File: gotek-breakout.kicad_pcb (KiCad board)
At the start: 2 copper layers, 90 x 20 mm, 4 parts, among them J1 FFC 10x1 0.5mm, J2 USB_A, J3 OLED, J4 Encoder

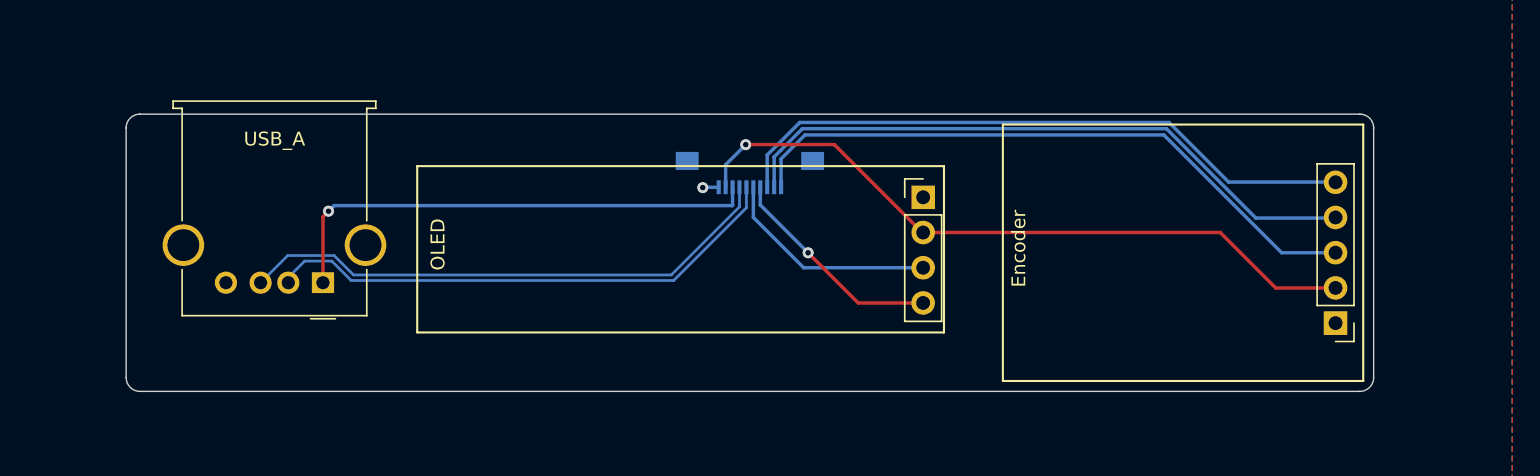
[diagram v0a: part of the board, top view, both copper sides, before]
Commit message: Make room for mounting
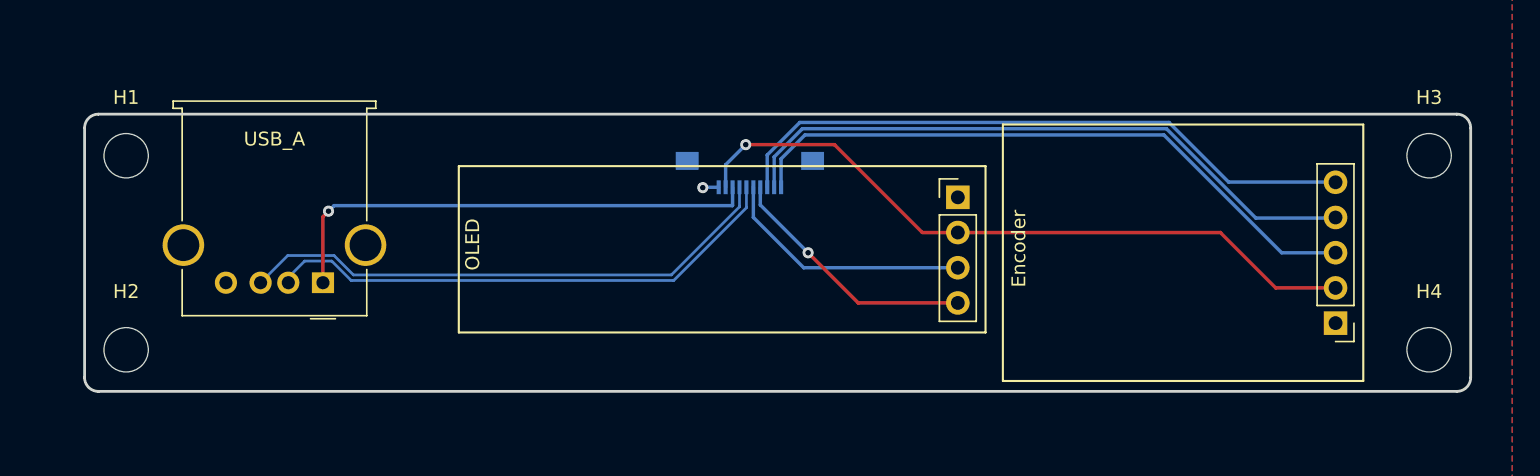
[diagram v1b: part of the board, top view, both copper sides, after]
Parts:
- added H1: MountingHole_3.2mm_M3, MountingHole:MountingHole_3.2mm_M3, F.Cu at (50.0, 43.0)
- added H2: MountingHole_3.2mm_M3, MountingHole:MountingHole_3.2mm_M3, F.Cu at (50.0, 57.0)
- added H3: MountingHole_3.2mm_M3, MountingHole:MountingHole_3.2mm_M3, F.Cu at (144.0, 43.0)
- added H4: MountingHole_3.2mm_M3, MountingHole:MountingHole_3.2mm_M3, F.Cu at (144.0, 57.0)
- moved J3 2.50 mm to (110.0, 46.0)
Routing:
- net /OLED_SCK: track 15.9 -> 18.4 mm
- net /OLED_SDA: track 16.0 -> 18.5 mm
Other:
- board size 90 x 20 mm -> 100 x 20 mm
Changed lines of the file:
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@@
     (pad "5" thru_hole circle (at 10.07 2.71 180) (size 3 3) (drill 2.3) (layers "*.Cu" "*.Mask")
       (net 1 "/GND") (pinfunction "Shield") (pintype "passive"))
-    (model "${KICAD6_3DMODEL_DIR}/Connector_USB.3dshapes/USB_A_Molex_67643_Horizontal.wrl"
-      (offset (xyz 0 0 0))
+    (model "${KICAD7_3DMODEL_DIR}/Connector_USB.3dshapes/USB_A_TE_292303-7_Horizontal.step"
+      (offset (xyz 3.5 -5.5 0))
       (scale (xyz 1 1 1))
       (rotate (xyz 0 0 0))
@@
     )
   )
+  (footprint "MountingHole:MountingHole_3.2mm_M3" (layer "F.Cu")
+    (at 50 43)
+    (descr "Mounting Hole 3.2mm, no annular, M3")
+    (tags "mounting hole 3.2mm no annular m3")
+    (clearance 1)
+    (attr board_only exclude_from_pos_files exclude_from_bom)
+    (fp_text reference "H1" (at 0 -4.2) (layer "F.SilkS")
+        (effects (font (size 1 1) (thickness 0.15)))
+    )
+    (fp_text value "MountingHole_3.2mm_M3" (at 0 4.2) (layer "F.Fab")
+        (effects (font (size 1 1) (thickness 0.15)))
+    )
+    (fp_text user "${REFERENCE}" (at 0 0) (layer "F.Fab")
+        (effects (font (size 1 1) (thickness 0.15)))
+    )
+    (fp_circle (center 0 0) (end 3.2 0)
+      (stroke (width 0.15) (type solid)) (fill none) (layer "Cmts.User"))
+    (fp_circle (center 0 0) (end 3.45 0)
+      (stroke (width 0.05) (type solid)) (fill none) (layer "F.CrtYd"))
+    (pad "" np_thru_hole circle (at 0 0) (size 3.2 3.2) (drill 3.2) (layers "*.Cu" "*.Mask"))
+  )
+  (footprint "MountingHole:MountingHole_3.2mm_M3" (layer "F.Cu")
+    (at 144 57)
+    (descr "Mounting Hole 3.2mm, no annular, M3")
+    (tags "mounting hole 3.2mm no annular m3")
+    (clearance 1)
+    (attr board_only exclude_from_pos_files exclude_from_bom)
+    (fp_text reference "H4" (at 0 -4.2) (layer "F.SilkS")
+        (effects (font (size 1 1) (thickness 0.15)))
+    )
+    (fp_text value "MountingHole_3.2mm_M3" (at 0 4.2) (layer "F.Fab")
+        (effects (font (size 1 1) (thickness 0.15)))
+    )
+    (fp_text user "${REFERENCE}" (at 0 0) (layer "F.Fab")
+        (effects (font (size 1 1) (thickness 0.15)))
+    )
+    (fp_circle (center 0 0) (end 3.2 0)
+      (stroke (width 0.15) (type solid)) (fill none) (layer "Cmts.User"))
+    (fp_circle (center 0 0) (end 3.45 0)
+      (stroke (width 0.05) (type solid)) (fill none) (layer "F.CrtYd"))
+    (pad "" np_thru_hole circle (at 0 0) (size 3.2 3.2) (drill 3.2) (layers "F&B.Cu" "*.Mask"))
+  )
   (footprint "Connector_PinHeader_2.54mm:PinHeader_1x04_P2.54mm_Vertical" (layer "F.Cu")
-    (at 107.5 46)
+    (at 110 46)
     (descr "Through hole straight pin header, 1x04, 2.54mm pitch, single row")
     (tags "Through hole pin header THT 1x04 2.54mm single row")
@@
       (rotate (xyz 0 0 0))
     )
+  )
+  (footprint "MountingHole:MountingHole_3.2mm_M3" (layer "F.Cu")
+    (at 144 43)
+    (descr "Mounting Hole 3.2mm, no annular, M3")
+    (tags "mounting hole 3.2mm no annular m3")
+    (clearance 1)
+    (attr board_only exclude_from_pos_files exclude_from_bom)
+    (fp_text reference "H3" (at 0 -4.2) (layer "F.SilkS")
+        (effects (font (size 1 1) (thickness 0.15)))
+    )
+    (fp_text value "MountingHole_3.2mm_M3" (at 0 4.2) (layer "F.Fab")
+        (effects (font (size 1 1) (thickness 0.15)))
+    )
+    (fp_text user "${REFERENCE}" (at 0 0) (layer "F.Fab")
+        (effects (font (size 1 1) (thickness 0.15)))
+    )
+    (fp_circle (center 0 0) (end 3.2 0)
+      (stroke (width 0.15) (type solid)) (fill none) (layer "Cmts.User"))
+    (fp_circle (center 0 0) (end 3.45 0)
+      (stroke (width 0.05) (type solid)) (fill none) (layer "F.CrtYd"))
+    (pad "" np_thru_hole circle (at 0 0) (size 3.2 3.2) (drill 3.2) (layers "*.Cu" "*.Mask"))
+  )
+  (footprint "MountingHole:MountingHole_3.2mm_M3" (layer "F.Cu")
+    (at 50 57)
+    (descr "Mounting Hole 3.2mm, no annular, M3")
+    (tags "mounting hole 3.2mm no annular m3")
+    (clearance 1)
+    (attr board_only exclude_from_pos_files exclude_from_bom)
+    (fp_text reference "H2" (at 0 -4.2) (layer "F.SilkS")
+        (effects (font (size 1 1) (thickness 0.15)))
+    )
+    (fp_text value "MountingHole_3.2mm_M3" (at 0 4.2) (layer "F.Fab")
+        (effects (font (size 1 1) (thickness 0.15)))
+    )
+    (fp_text user "${REFERENCE}" (at 0 0) (layer "F.Fab")
+        (effects (font (size 1 1) (thickness 0.15)))
+    )
+    (fp_circle (center 0 0) (end 3.2 0)
+      (stroke (width 0.15) (type solid)) (fill none) (layer "Cmts.User"))
+    (fp_circle (center 0 0) (end 3.45 0)
+      (stroke (width 0.05) (type solid)) (fill none) (layer "F.CrtYd"))
+    (pad "" np_thru_hole circle (at 0 0) (size 3.2 3.2) (drill 3.2) (layers "F&B.Cu" "*.Mask"))
   )
   (footprint "Connector_FFC-FPC:Molex_54548-1071_1x10-1MP_P0.5mm_Horizontal" (layer "B.Cu")
@@
     (pad "MP" smd rect (at -4.525 -0.875) (size 1.65 1.3) (layers "B.Cu" "B.Paste" "B.Mask"))
     (pad "MP" smd rect (at 4.525 -0.875) (size 1.65 1.3) (layers "B.Cu" "B.Paste" "B.Mask"))
-    (model "${KICAD6_3DMODEL_DIR}/Connector_FFC-FPC.3dshapes/Molex_54548-1071_1x10-1MP_P0.5mm_Horizontal.wrl"
-      (offset (xyz 0 0 0))
+    (model "${KICAD7_3DMODEL_DIR}/Connector_FFC-FPC.3dshapes/Hirose_FH12-10S-0.5SH_1x10-1MP_P0.50mm_Horizontal.step"
+      (offset (xyz 0 -0.5 0))
       (scale (xyz 1 1 1))
       (rotate (xyz 0 0 0))
     )
   )
-  (gr_rect (start 71 43.75) (end 109 55.75)
+  (gr_rect (start 74 43.75) (end 112 55.75)
     (stroke (width 0.15) (type default)) (fill none) (layer "F.SilkS"))
   (gr_rect (start 113.25 40.75) (end 139.25 59.25)
     (stroke (width 0.15) (type default)) (fill none) (layer "F.SilkS"))
-  (gr_arc (start 140 59) (mid 139.707107 59.707107) (end 139 60)
-    (stroke (width 0.1) (type default)) (layer "Edge.Cuts"))
-  (gr_line (start 140 41) (end 140 59)
-    (stroke (width 0.1) (type default)) (layer "Edge.Cuts"))
-  (gr_line (start 50 59) (end 50 41)
-    (stroke (width 0.1) (type default)) (layer "Edge.Cuts"))
-  (gr_arc (start 51 60) (mid 50.292893 59.707107) (end 50 59)
-    (stroke (width 0.1) (type default)) (layer "Edge.Cuts"))
-  (gr_arc (start 139 40) (mid 139.707107 40.292893) (end 140 41)
-    (stroke (width 0.1) (type default)) (layer "Edge.Cuts"))
-  (gr_arc (start 50 41) (mid 50.292893 40.292893) (end 51 40)
-    (stroke (width 0.1) (type default)) (layer "Edge.Cuts"))
-  (gr_line (start 51 40) (end 139 40)
-    (stroke (width 0.1) (type default)) (layer "Edge.Cuts"))
-  (gr_line (start 139 60) (end 51 60)
-    (stroke (width 0.1) (type default)) (layer "Edge.Cuts"))
+  (gr_line (start 47 59) (end 47 41)
+    (stroke (width 0.2) (type default)) (layer "Edge.Cuts"))
+  (gr_line (start 147 41) (end 147 59)
+    (stroke (width 0.2) (type default)) (layer "Edge.Cuts"))
+  (gr_line (start 146 60) (end 48 60)
+    (stroke (width 0.2) (type default)) (layer "Edge.Cuts"))
+  (gr_arc (start 47 41) (mid 47.292893 40.292893) (end 48 40)
+    (stroke (width 0.2) (type default)) (layer "Edge.Cuts"))
+  (gr_arc (start 48 60) (mid 47.292893 59.707107) (end 47 59)
+    (stroke (width 0.2) (type default)) (layer "Edge.Cuts"))
+  (gr_line (start 48 40) (end 146 40)
+    (stroke (width 0.2) (type default)) (layer "Edge.Cuts"))
+  (gr_arc (start 146 40) (mid 146.707107 40.292893) (end 147 41)
+    (stroke (width 0.2) (type default)) (layer "Edge.Cuts"))
+  (gr_arc (start 147 59) (mid 146.707107 59.707107) (end 146 60)
+    (stroke (width 0.2) (type default)) (layer "Edge.Cuts"))
   (via (at 91.6 45.3) (size 0.8) (drill 0.4) (layers "F.Cu" "B.Cu") (net 1))
   (segment (start 91.625 45.275) (end 91.6 45.3) (width 0.25) (layer "B.Cu") (net 1))
   (segment (start 92.75 45.275) (end 91.625 45.275) (width 0.25) (layer "B.Cu") (net 1))
+  (segment (start 128.94 48.54) (end 132.935 52.535) (width 0.25) (layer "F.Cu") (net 2))
+  (segment (start 110 48.54) (end 128.94 48.54) (width 0.25) (layer "F.Cu") (net 2))
+  (segment (start 101.1 42.2) (end 107.44 48.54) (width 0.25) (layer "F.Cu") (net 2))
   (segment (start 94.7 42.2) (end 101.1 42.2) (width 0.25) (layer "F.Cu") (net 2))
-  (segment (start 101.1 42.2) (end 107.44 48.54) (width 0.25) (layer "F.Cu") (net 2))
-  (segment (start 128.94 48.54) (end 132.935 52.535) (width 0.25) (layer "F.Cu") (net 2))
-  (segment (start 107.5 48.54) (end 128.94 48.54) (width 0.25) (layer "F.Cu") (net 2))
   (segment (start 132.935 52.535) (end 137.25 52.535) (width 0.25) (layer "F.Cu") (net 2))
-  (segment (start 107.44 48.54) (end 107.5 48.54) (width 0.25) (layer "F.Cu") (net 2))
+  (segment (start 107.44 48.54) (end 110 48.54) (width 0.25) (layer "F.Cu") (net 2))
   (via (at 94.7 42.2) (size 0.8) (drill 0.4) (layers "F.Cu" "B.Cu") (net 2))
   (segment (start 93.25 45.275) (end 93.25 43.65) (width 0.25) (layer "B.Cu") (net 2))
@@
   (segment (start 64.834315 50.6) (end 66.234315 52) (width 0.2) (layer "B.Cu") (net 5))
   (segment (start 95.25 45.275) (end 95.25 47.45) (width 0.25) (layer "B.Cu") (net 6))
+  (segment (start 98.88 51.08) (end 110 51.08) (width 0.25) (layer "B.Cu") (net 6))
   (segment (start 95.25 47.45) (end 98.88 51.08) (width 0.25) (layer "B.Cu") (net 6))
-  (segment (start 98.88 51.08) (end 107.5 51.08) (width 0.25) (layer "B.Cu") (net 6))
   (segment (start 99.2 50) (end 102.82 53.62) (width 0.25) (layer "F.Cu") (net 7))
-  (segment (start 102.82 53.62) (end 107.5 53.62) (width 0.25) (layer "F.Cu") (net 7))
+  (segment (start 102.82 53.62) (end 110 53.62) (width 0.25) (layer "F.Cu") (net 7))
   (via (at 99.2 50) (size 0.8) (drill 0.4) (layers "F.Cu" "B.Cu") (net 7))
   (segment (start 95.75 46.55) (end 95.75 45.275) (width 0.25) (layer "B.Cu") (net 7))

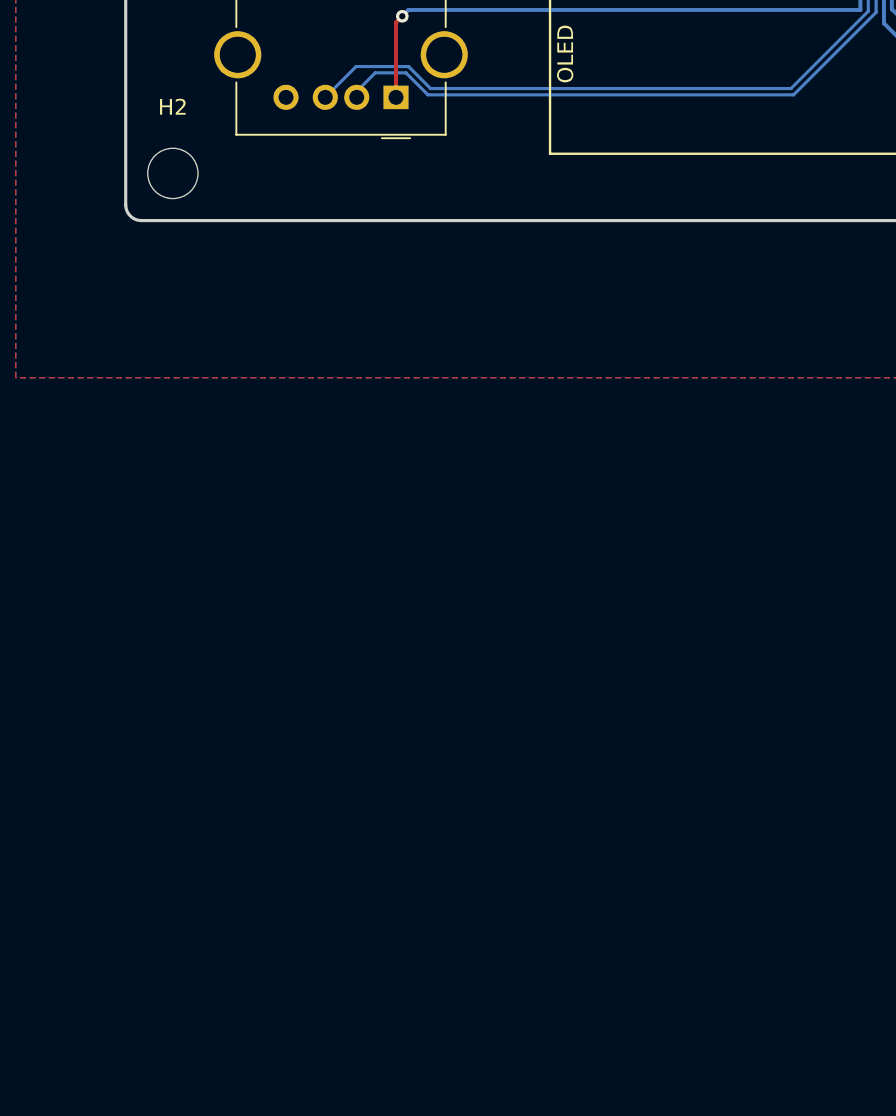
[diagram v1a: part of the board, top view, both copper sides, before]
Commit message: Add adapter piece, need to work out mounting
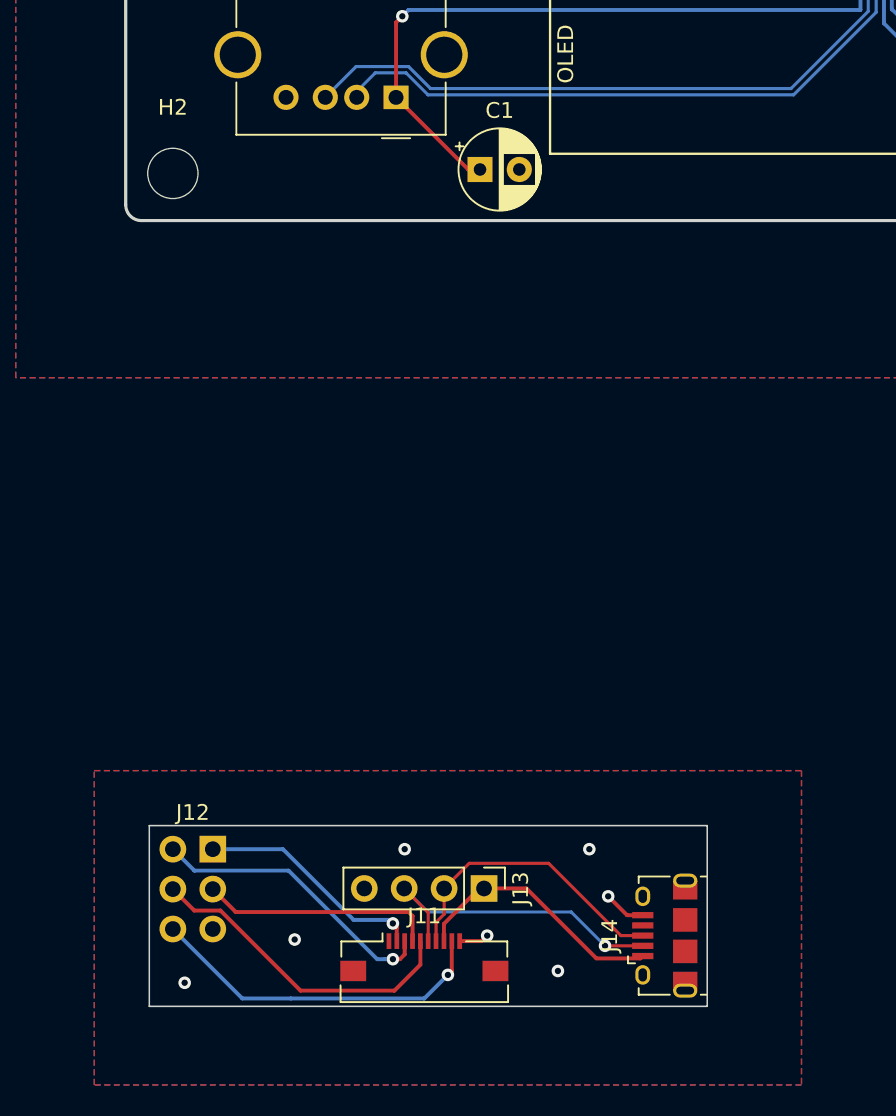
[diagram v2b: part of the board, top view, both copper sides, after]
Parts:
- added C1: 22u, Capacitor_THT:CP_Radial_D5.0mm_P2.50mm, F.Cu at (69.5, 56.8)
- added J11: FFC 10x1 0.5mm, Connector_FFC-FPC:Molex_54548-1071_1x10-1MP_P0.5mm_Horizontal, F.Cu at (66.0, 106.9)
- added J12: Gotek 6-pin connector, Connector_PinHeader_2.54mm:PinHeader_2x03_P2.54mm_Vertical, F.Cu at (50.0, 100.0)
- added J13: USB Breakout, Connector_PinHeader_2.54mm:PinHeader_1x04_P2.54mm_Vertical, F.Cu at (69.8, 102.5)
- added J14: USB_B_Micro, Connector_USB:USB_Micro-B_Amphenol_10118194_Horizontal, F.Cu at (81.3, 105.5)
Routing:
- net /Gotek Side/VCC: track 0.00 -> 22.2 mm, vias 0 -> 1
- net /Gotek Side/USB_D-: track 0.00 -> 20.7 mm, vias 0 -> 1
- net /Gotek Side/OLED_SCK: track 0.00 -> 20.6 mm
- net /Gotek Side/USB_D+: track 0.00 -> 18.8 mm
- net /Gotek Side/ROT_CLK: track 0.00 -> 18.6 mm, vias 0 -> 1
- net /Gotek Side/USB_VIN: track 0.00 -> 16.6 mm
- net /Gotek Side/OLED_SDA: track 0.00 -> 15.0 mm
- net /Gotek Side/ROT_DT: track 0.00 -> 14.6 mm, vias 0 -> 1
- net /USB_VIN: track 36.0 -> 43.2 mm
- net /Gotek Side/GND: track 0.00 -> 4.59 mm, vias 0 -> 7
- added copper zone on B.Cu, net /Gotek Side/GND
- added copper zone on F.Cu, net /Gotek Side/GND
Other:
- board size 100 x 20 mm -> 100 x 70 mm
